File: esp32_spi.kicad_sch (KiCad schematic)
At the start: 27 parts, among them J1 Conn_01x06_Female, SW1 SW_Push, SW2 SW_Push, U201 SN74LV1T34, U202 SN74LV1T34, U203 74AHCT595, U204 SN74LV1T34, U205 74AHCT595, U206 ESP32-WROOM-32, U207 74AHCT595

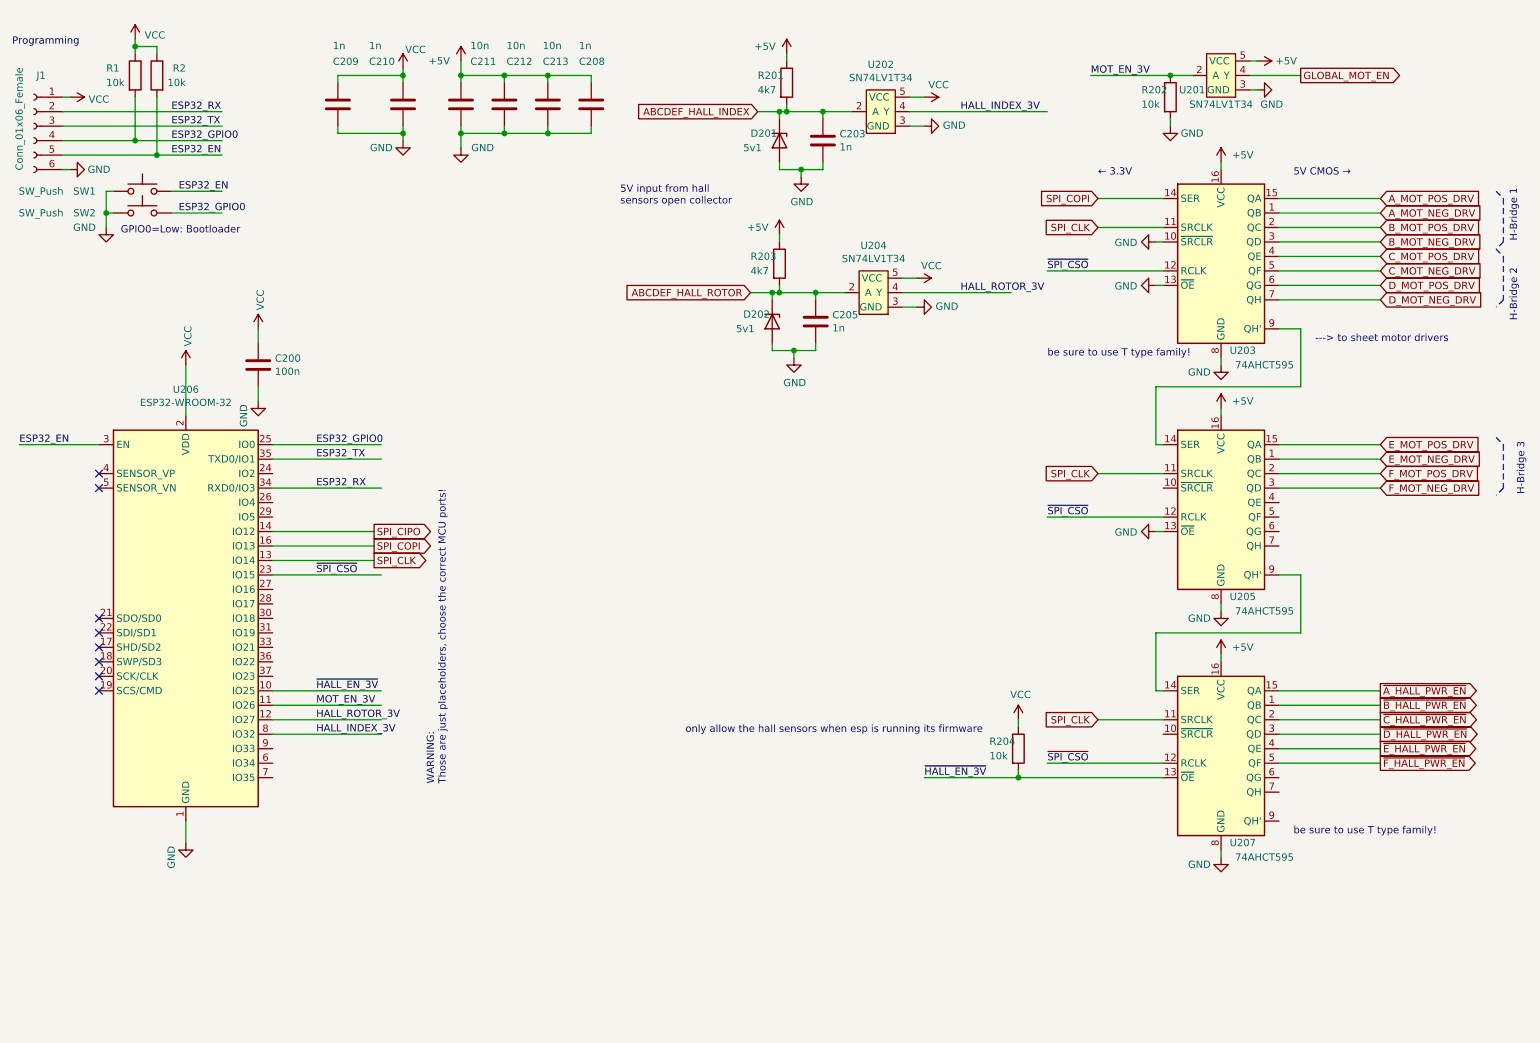
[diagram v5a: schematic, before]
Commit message: esp32_shiftregs: add comments and labels to esp32 pins
Additional remarks for pin use, pullup on ~CS0 (also
relevant during boot of esp32)
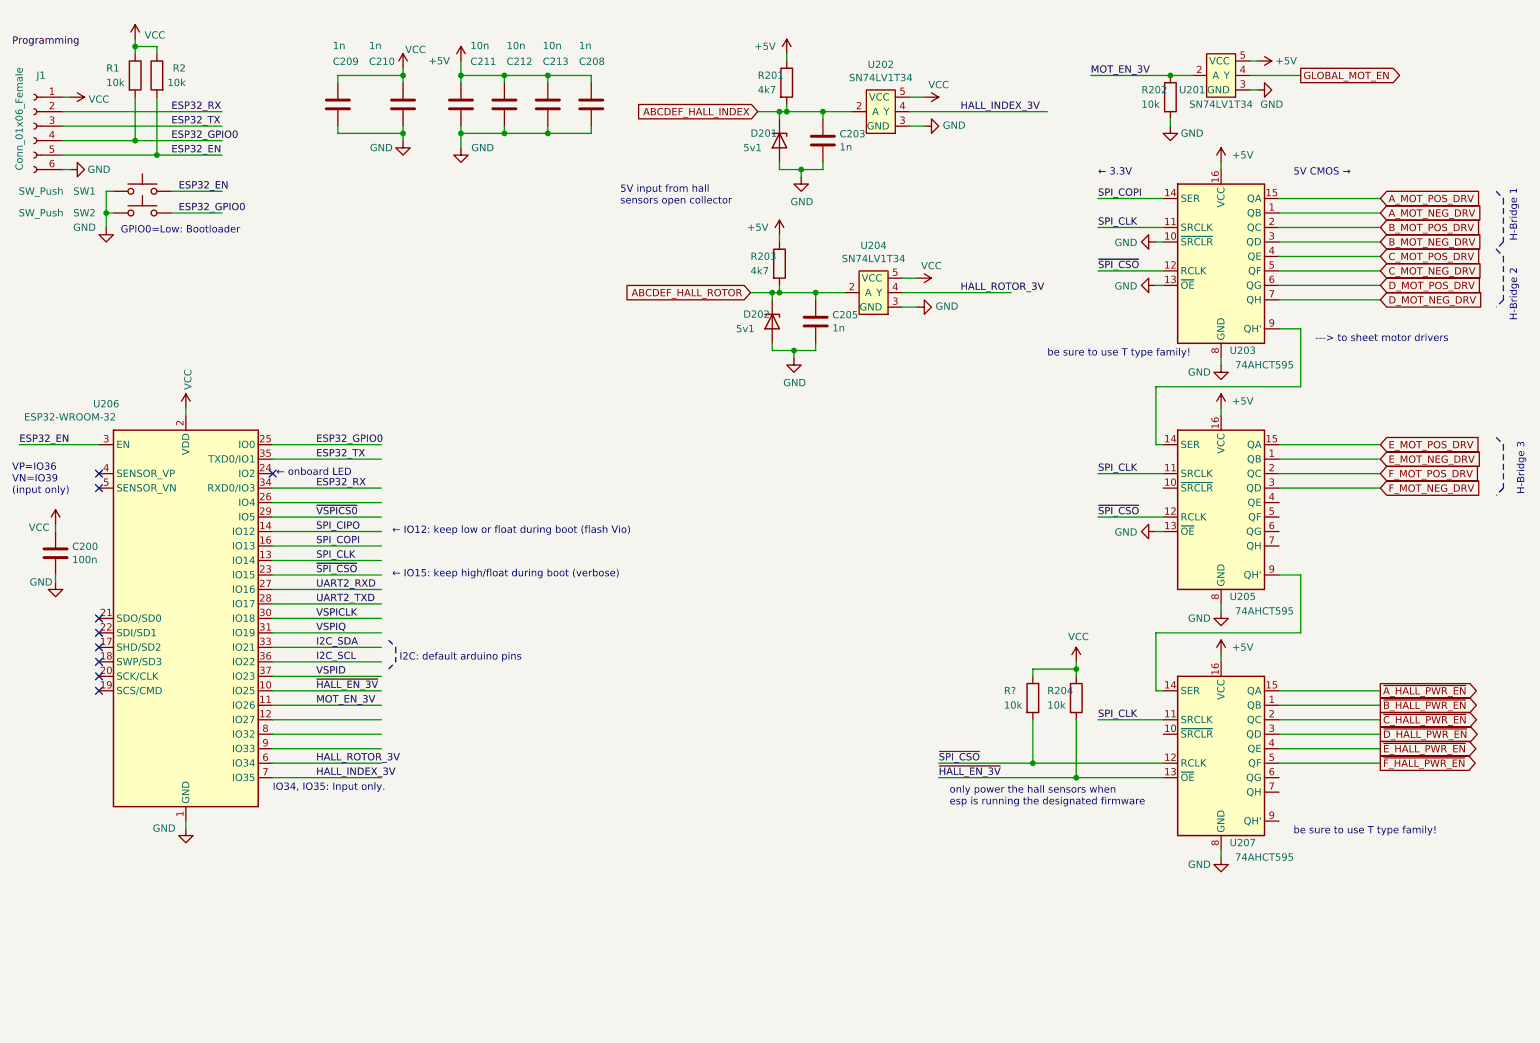
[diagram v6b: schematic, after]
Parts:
- added R?: 10k, Resistor_SMD:R_0603_1608Metric, symbol Device:R
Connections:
- net HALL_INDEX_3V: now also U206.7 (IO35); no longer U206.8 (IO32)
- net HALL_ROTOR_3V: now also U206.6 (IO34); no longer U206.12 (IO27)
- net VCC: now also R?.1
- net ~SPI_CSO~: now also R?.2
- net UART2_RXD: now reaches U206.27 (IO16)
- net UART2_TXD: now reaches U206.28 (IO17)
- net ~VSPICS0~: now reaches U206.29 (IO5)
- net VSPICLK: now reaches U206.30 (IO18)
- net VSPIQ: now reaches U206.31 (IO19)
- net I2C_SDA: now reaches U206.33 (IO21)
- net I2C_SCL: now reaches U206.36 (IO22)
- net VSPID: now reaches U206.37 (IO23)
- no-connect marks 8 -> 9
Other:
- note added: "I2C: default arduino pins"
- note added: "IO34, IO35: Input only."
- note added: "VP=IO36 VN=IO39 (input only)"
- note added: "only power the hall sensors when esp is running the designated firmware"
- note added: "← IO12: keep low or float during boot (flash Vio)"
- note added: "← IO15: keep high/float during boot (verbose)"
- note added: "← onboard LED"
- note removed: "WARNING: Those are just placeholders, choose the correct MCU ports!"
- note removed: "only allow the hall sensors when esp is running its firmware"
- moved on the sheet: C200, R204

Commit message: esp32/shiftreg: add connector for ext. controller
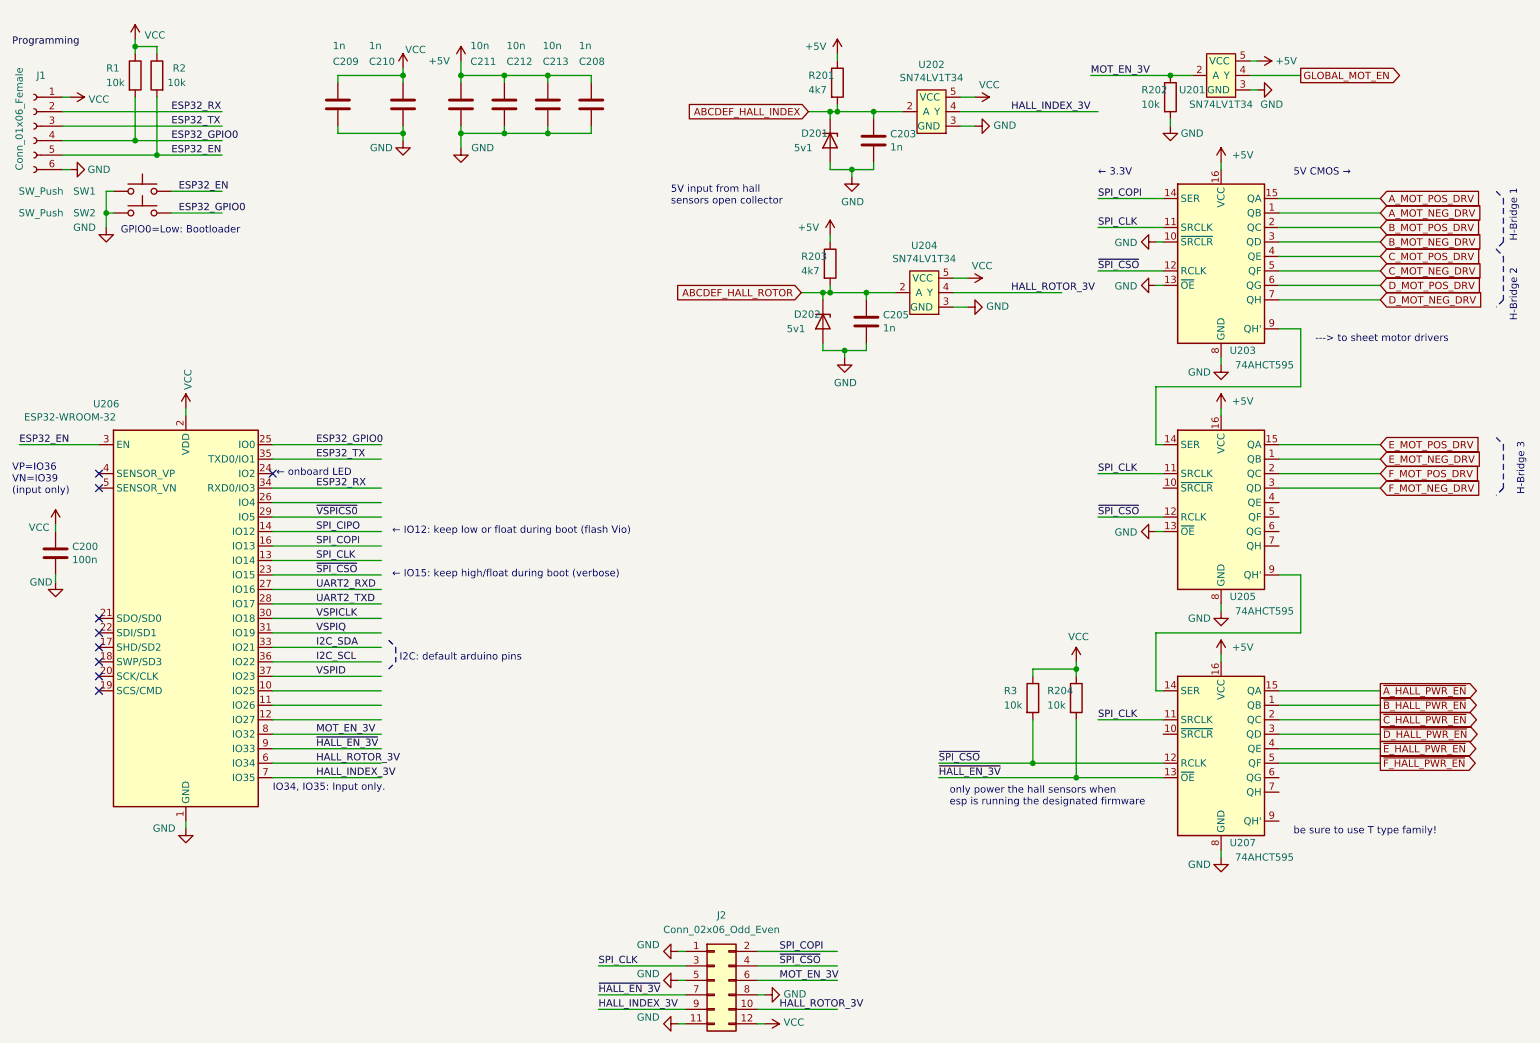
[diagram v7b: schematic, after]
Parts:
- added J2: Conn_02x06_Odd_Even, Connector_PinHeader_2.54mm:PinHeader_2x06_P2.54mm_Vertical, symbol Connector_Generic:Conn_02x06_Odd_Even
- gave numbers to parts that had none: 1
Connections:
- net GND: now also J2.1 (Pin_1), J2.11 (Pin_11), J2.5 (Pin_5), J2.8 (Pin_8)
- net HALL_INDEX_3V: now also J2.9 (Pin_9)
- net HALL_ROTOR_3V: now also J2.10 (Pin_10)
- net MOT_EN_3V: now also U206.8 (IO32), J2.6 (Pin_6); no longer U206.11 (IO26)
- net SPI_CLK: now also J2.3 (Pin_3)
- net SPI_COPI: now also J2.2 (Pin_2)
- net VCC: now also J2.12 (Pin_12)
- net ~HALL_EN_3V~: now also U206.9 (IO33), J2.7 (Pin_7); no longer U206.10 (IO25)
- net ~SPI_CSO~: now also J2.4 (Pin_4)
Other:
- moved on the sheet: C203, C205, D201, D202, R201, R203, U202, U204

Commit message: Zener diodes now 5v6
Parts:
- D201, D202: value 5v1 -> 5v6; Link https://www.reichelt.de/zenerdiode-5-1-v-0-35-w-sot-23-smd-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 -> https://www.reichelt.de/zenerdiode-5-6-v-0-35-w-sot-23-smd-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
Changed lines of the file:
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@@
   (junction (at 204.47 147.32) (diameter 1.016) (color 0 0 0 0))
   (junction (at 220.98 24.13) (diameter 1.016) (color 0 0 0 0))
+  (no_connect (at 33.02 127))
+  (no_connect (at 33.02 129.54))
+  (no_connect (at 33.02 96.52))
+  (no_connect (at 33.02 132.08))
+  (no_connect (at 33.02 124.46))
   (no_connect (at 33.02 121.92))
-  (no_connect (at 33.02 132.08))
-  (no_connect (at 33.02 129.54))
-  (no_connect (at 33.02 124.46))
   (no_connect (at 33.02 119.38))
   (no_connect (at 33.02 93.98))
-  (no_connect (at 33.02 96.52))
   (no_connect (at 63.5 93.98))
-  (no_connect (at 33.02 127))
   (wire (pts (xy 19.05 88.9) (xy 33.02 88.9))
     (stroke (width 0) (type solid) (color 0 0 0 0))
@@
       (effects (font (size 1.27 1.27)) (justify left))
     )
-    (property "Value" "5v1" (id 1) (at 153.67 68.58 90)
+    (property "Value" "5v6" (id 1) (at 153.67 68.58 90)
       (effects (font (size 1.27 1.27)) (justify left))
     )
@@
       (effects (font (size 1.27 1.27)) hide)
     )
-    (property "Link" "https://www.reichelt.de/zenerdiode-5-1-v-0-35-w-sot-23-smd-zd-5-1-p18916.html?&trstct=pos_3&nbc=1" (id 5) (at 160.02 67.31 0)
+    (property "Link" "https://www.reichelt.de/zenerdiode-5-6-v-0-35-w-sot-23-smd-zd-5-6-p18917.html?&trstct=pos_0&nbc=1" (id 5) (at 160.02 67.31 0)
       (effects (font (size 1.27 1.27)) hide)
     )
@@
       (effects (font (size 1.27 1.27)) (justify left))
     )
-    (property "Value" "5v1" (id 1) (at 154.94 36.83 90)
+    (property "Value" "5v6" (id 1) (at 154.94 36.83 90)
       (effects (font (size 1.27 1.27)) (justify left))
     )
@@
       (effects (font (size 1.27 1.27)) hide)
     )
-    (property "Link" "https://www.reichelt.de/zenerdiode-5-1-v-0-35-w-sot-23-smd-zd-5-1-p18916.html?&trstct=pos_3&nbc=1" (id 5) (at 161.29 35.56 0)
-      (effects (font (size 1.27 1.27)) hide)
-    )
+    (property "Link" "https://www.reichelt.de/zenerdiode-5-6-v-0-35-w-sot-23-smd-zd-5-6-p18917.html?&trstct=pos_0&nbc=1" (id 5) (at 161.29 35.56 0)
+      (effects (font (size 1.27 1.27)) hide)
+    )
